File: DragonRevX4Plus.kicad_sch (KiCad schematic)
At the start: 22 parts, among them J14 PWR_LED, J15 PWR_SWITCH, J7 COMPOSITE, U1 TSN 1-2450

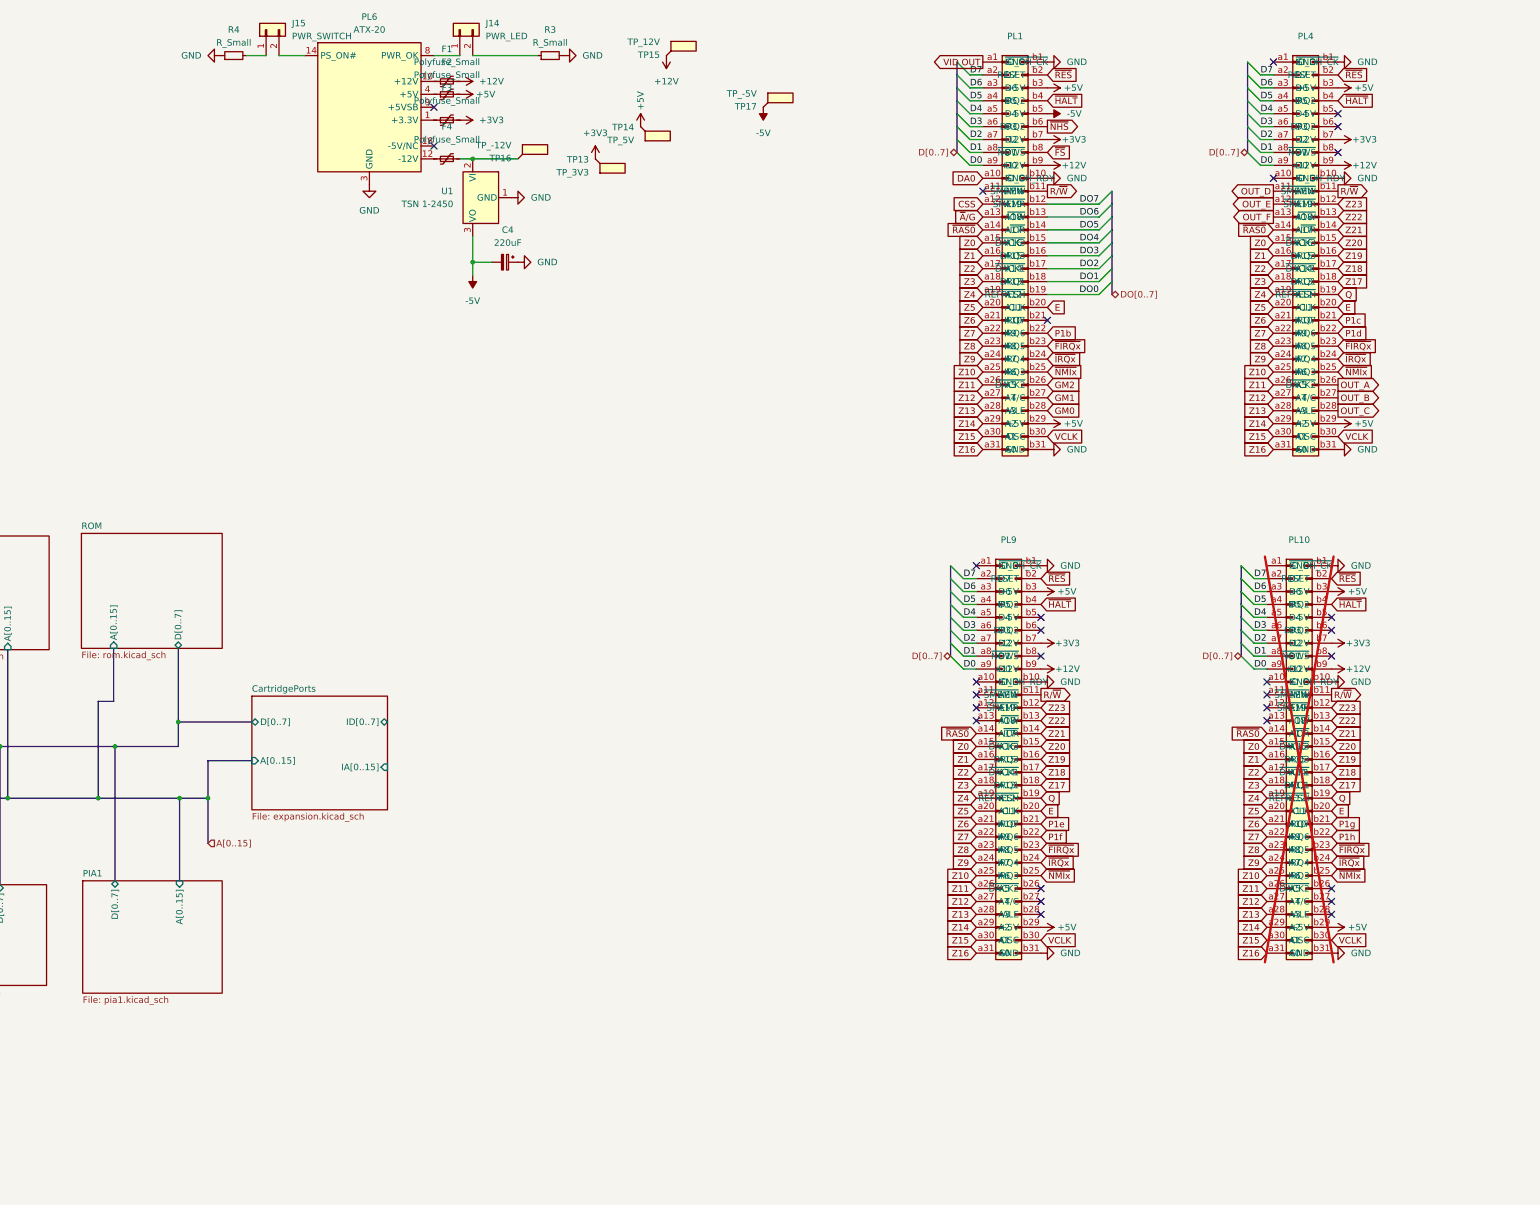
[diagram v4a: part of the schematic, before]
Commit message: add slot identification
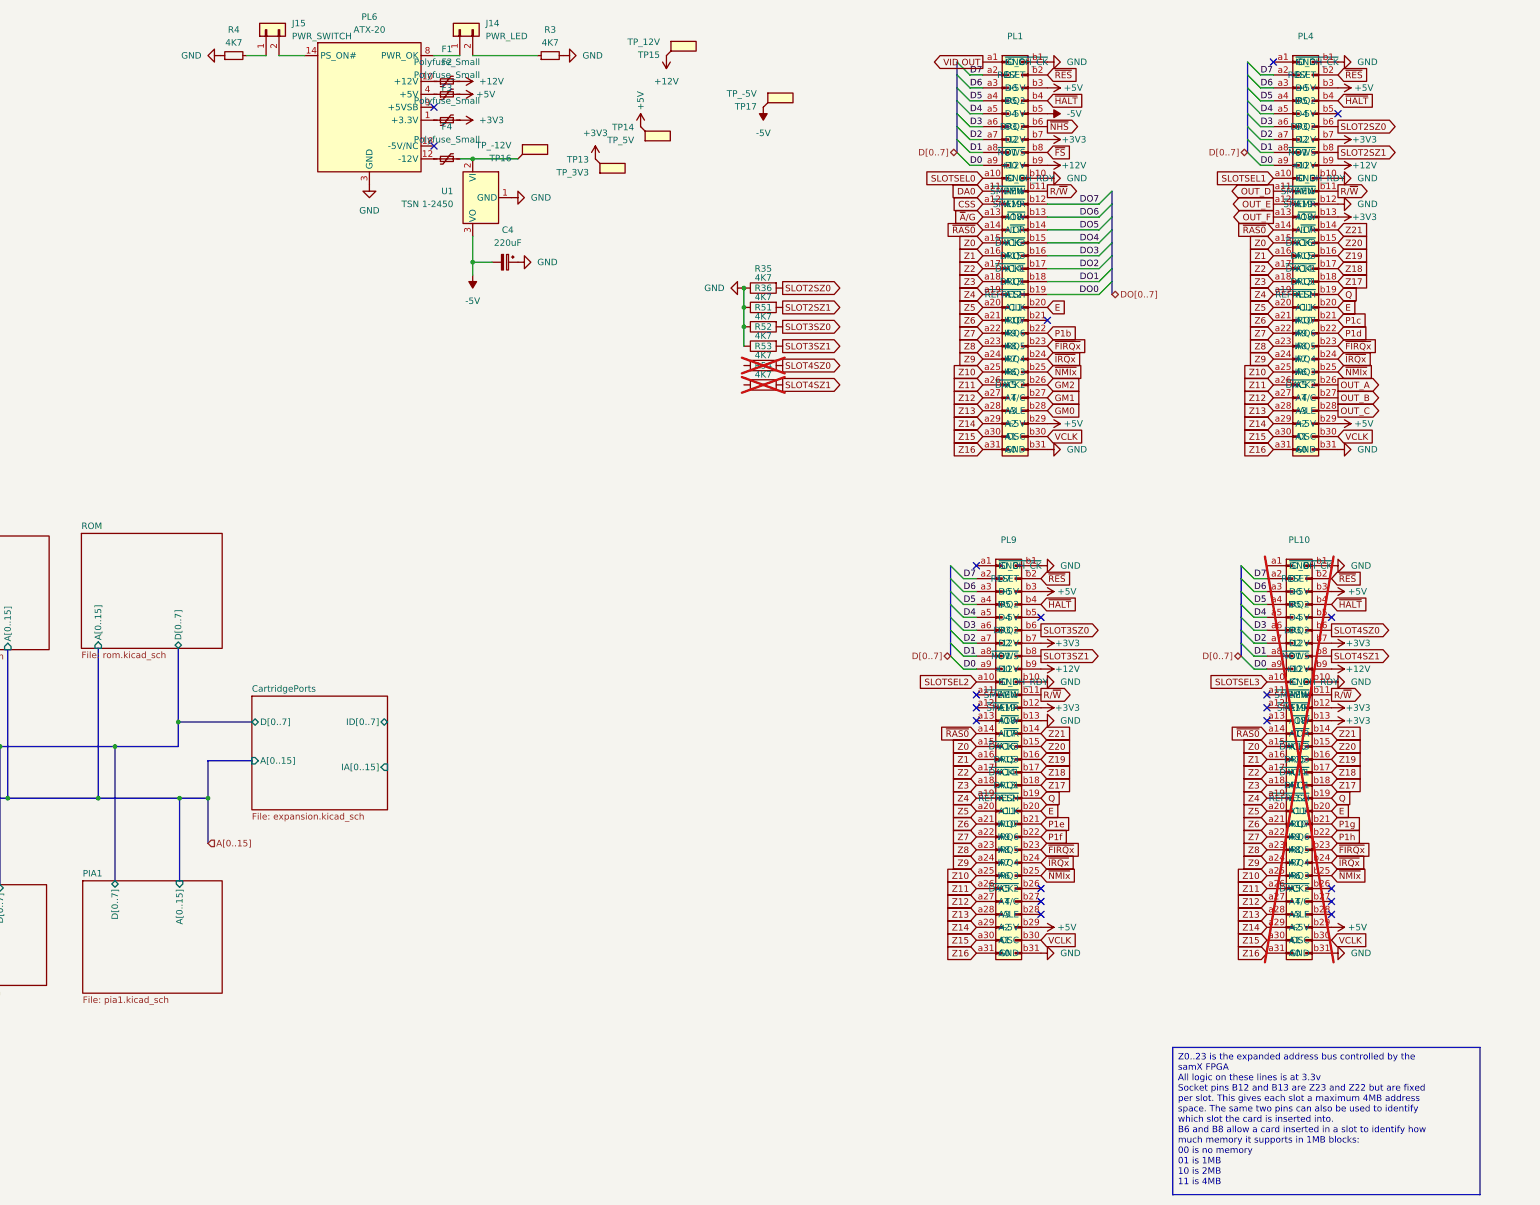
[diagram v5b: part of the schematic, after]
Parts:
- added R35, R36, R51, R52, R53, R54: 4K7, Resistor_SMD:R_0805_2012Metric_Pad1.20x1.40mm_HandSolder, symbol Device:R
- R3, R4: value R_Small -> 4K7
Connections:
- net +3V3: now also PL10.b12 (~{SMEMR}), PL10.b13 (~{IOW}), PL4.b13 (~{IOW}), PL9.b12 (~{SMEMR})
- net DA0: now also PL1.a11 (AEN); no longer PL1.a10 (IO_CH_RDY)
- net GND: now also PL4.b12 (~{SMEMR}), PL9.b13 (~{IOW}), R35.1, R36.1, R51.1, R52.1
- net SLOTSEL3: now reaches PL10.a10 (IO_CH_RDY)
- net SLOT4SZ0: now reaches PL10.b6 (DRQ2)
- net SLOT4SZ0: now also R53.2
- net SLOT4SZ1: now reaches PL10.b8 (~{NOWS})
- net SLOT4SZ1: now also R54.2
- net SLOTSEL2: now reaches PL9.a10 (IO_CH_RDY)
- net SLOT3SZ0: now reaches PL9.b6 (DRQ2)
- net SLOT3SZ0: now also R51.2
- net SLOT3SZ1: now reaches PL9.b8 (~{NOWS})
- net SLOT3SZ1: now also R52.2
- net SLOTSEL1: now reaches PL4.a10 (IO_CH_RDY)
- net SLOT2SZ0: now reaches PL4.b6 (DRQ2)
- net SLOT2SZ0: now also R35.2
- net SLOT2SZ1: now reaches PL4.b8 (~{NOWS})
- net SLOT2SZ1: now also R36.2
- removed net Z22: PL10.b13 (~{IOW}), PL4.b13 (~{IOW}), PL9.b13 (~{IOW})
- removed net Z23: PL10.b12 (~{SMEMR}), PL4.b12 (~{SMEMR}), PL9.b12 (~{SMEMR})
- new net SLOTSEL0: PL1.a10 (IO_CH_RDY)
- no-connect marks 30 -> 20

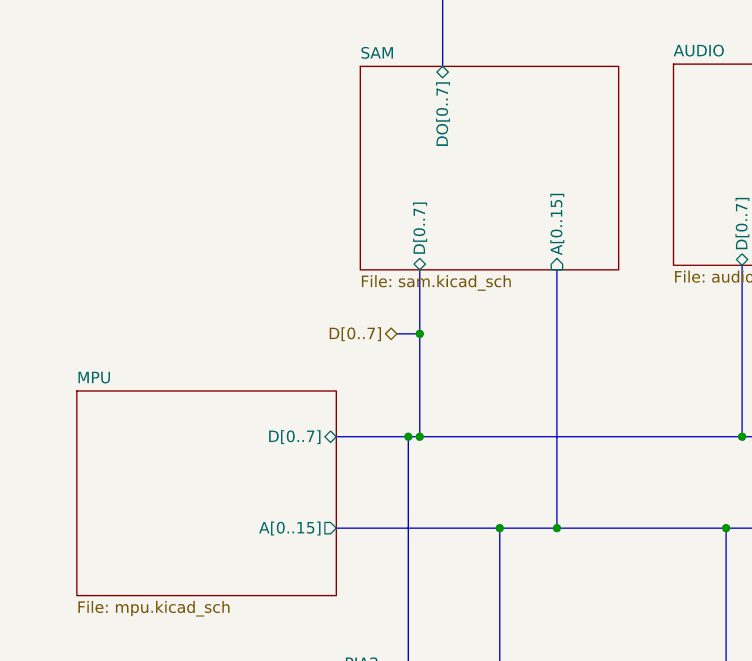
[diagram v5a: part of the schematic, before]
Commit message: add data bus transceiver
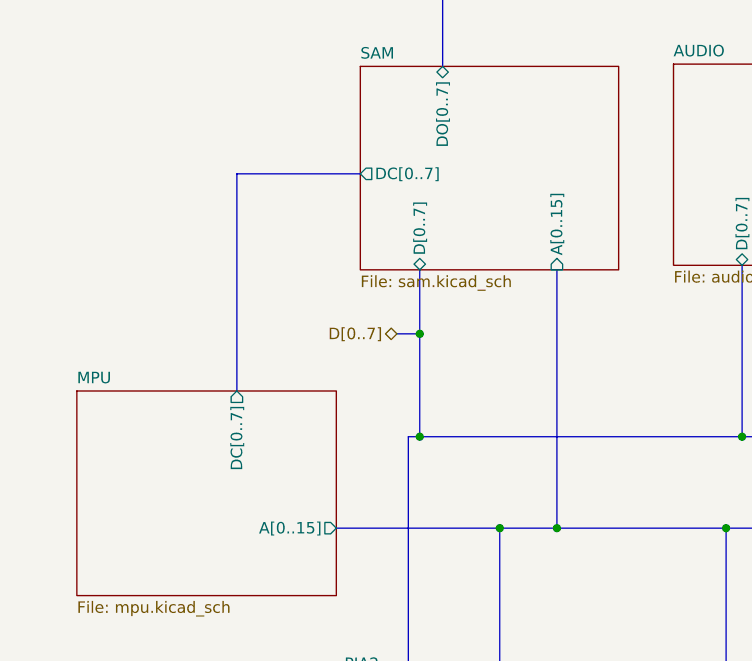
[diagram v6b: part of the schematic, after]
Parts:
- C4: DigiKey (none) -> 732-875575345004CT-ND
- R3, R35, R36, R4, R51, R52, R53, R54: DigiKey (none) -> 541-4131-1-ND
- U1: DigiKey (none) -> TSN1-2450-ND
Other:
- sheet MPU ports: added DC[0..7]; removed D[0..7]
- sheet SAM ports: added DC[0..7]; removed none
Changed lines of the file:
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@@
 	)
 	(junction
-		(at 64.77 160.02)
-		(diameter 0)
-		(color 0 0 0 0)
-	)
-	(junction
 		(at 66.04 148.59)
 		(diameter 0)
@@
 		)
 	)
+	(bus
+		(pts
+			(xy 45.72 154.94) (xy 45.72 130.81)
+		)
+		(stroke
+			(width 0)
+			(type default)
+		)
+	)
 	(wire
 		(pts
@@
 	(bus
 		(pts
-			(xy 56.769 160.02) (xy 64.77 160.02)
-		)
-		(stroke
-			(width 0)
-			(type default)
-		)
-	)
-	(bus
-		(pts
 			(xy 356.87 38.1) (xy 356.87 40.64)
 		)
@@
 	(bus
 		(pts
+			(xy 45.72 130.81) (xy 59.436 130.81)
+		)
+		(stroke
+			(width 0)
+			(type default)
+		)
+	)
+	(bus
+		(pts
 			(xy 355.6 132.08) (xy 355.6 129.54)
 		)
@@
 			)
 		)
+		(property "DigiKey" "541-4131-1-ND"
+			(at 261.62 77.47 90)
+			(effects
+				(font
+					(size 1.27 1.27)
+				)
+				(hide yes)
+			)
+		)
 		(pin "1"
 		)
@@
 			)
 		)
+		(property "DigiKey" "541-4131-1-ND"
+			(at 261.62 88.9 90)
+			(effects
+				(font
+					(size 1.27 1.27)
+				)
+				(hide yes)
+			)
+		)
 		(pin "1"
 		)
@@
 			)
 		)
+		(property "DigiKey" "541-4131-1-ND"
+			(at 261.62 73.66 90)
+			(effects
+				(font
+					(size 1.27 1.27)
+				)
+				(hide yes)
+			)
+		)
 		(pin "1"
 		)
@@
 			)
 		)
+		(property "DigiKey" "541-4131-1-ND"
+			(at 157.48 24.13 90)
+			(effects
+				(font
+					(size 1.27 1.27)
+				)
+				(hide yes)
+			)
+		)
 		(pin "2"
 		)
@@
 			)
 		)
+		(property "DigiKey" "541-4131-1-ND"
+			(at 261.62 85.09 90)
+			(effects
+				(font
+					(size 1.27 1.27)
+				)
+				(hide yes)
+			)
+		)
 		(pin "1"
 		)
@@
 			)
 		)
+		(property "DigiKey" "TSN1-2450-ND"
+			(at 204.47 52.07 90)
+			(effects
+				(font
+					(size 1.27 1.27)
+				)
+				(hide yes)
+			)
+		)
 		(pin "3"
 		)
@@
 			)
 		)
+		(property "DigiKey" "541-4131-1-ND"
+			(at 261.62 69.85 90)
+			(effects
+				(font
+					(size 1.27 1.27)
+				)
+				(hide yes)
+			)
+		)
 		(pin "1"
 		)
@@
 			)
 		)
+		(property "DigiKey" "732-875575345004CT-ND"
+			(at 210.82 64.77 90)
+			(effects
+				(font
+					(size 1.27 1.27)
+				)
+				(hide yes)
+			)
+		)
 		(pin "1"
 		)
@@
 			)
 		)
+		(property "DigiKey" "541-4131-1-ND"
+			(at 261.62 81.28 90)
+			(effects
+				(font
+					(size 1.27 1.27)
+				)
+				(hide yes)
+			)
+		)
 		(pin "1"
 		)
@@
 			)
 		)
+		(property "DigiKey" "541-4131-1-ND"
+			(at 219.71 24.13 90)
+			(effects
+				(font
+					(size 1.27 1.27)
+				)
+				(hide yes)
+			)
+		)
 		(pin "2"
 		)
@@
 			)
 		)
+		(pin "DC[0..7]" output
+			(at 59.436 130.81 180)
+			(effects
+				(font
+					(size 1.27 1.27)
+				)
+				(justify left)
+			)
+		)
 		(instances
 			(project "DragonRevX4Plus"
@@
 			)
 		)
-		(pin "D[0..7]" bidirectional
-			(at 56.769 160.02 0)
+		(pin "A[0..15]" output
+			(at 56.769 170.18 0)
 			(effects
 				(font
@@
 			)
 		)
-		(pin "A[0..15]" output
-			(at 56.769 170.18 0)
+		(pin "DC[0..7]" output
+			(at 45.72 154.94 90)
 			(effects
 				(font
